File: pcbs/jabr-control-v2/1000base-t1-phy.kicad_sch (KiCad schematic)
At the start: 17 parts, among them U8001 LAN8870, Y8001 XRCGB25M000F3A16R0

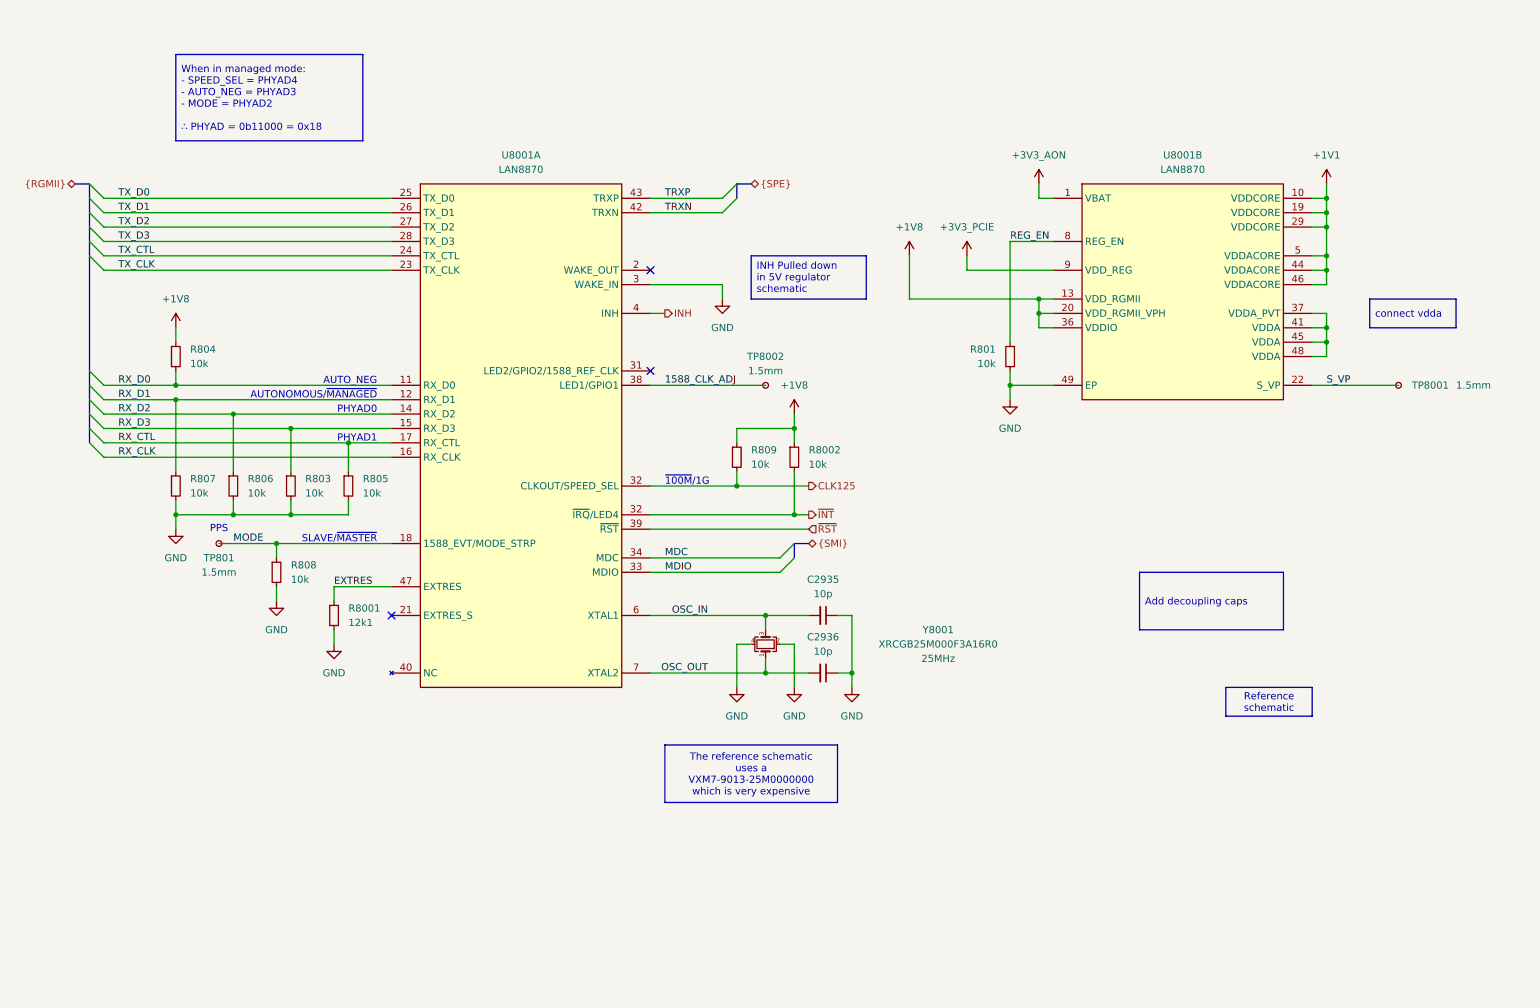
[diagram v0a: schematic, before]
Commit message: PCI11010C Schematic sheet mostly done
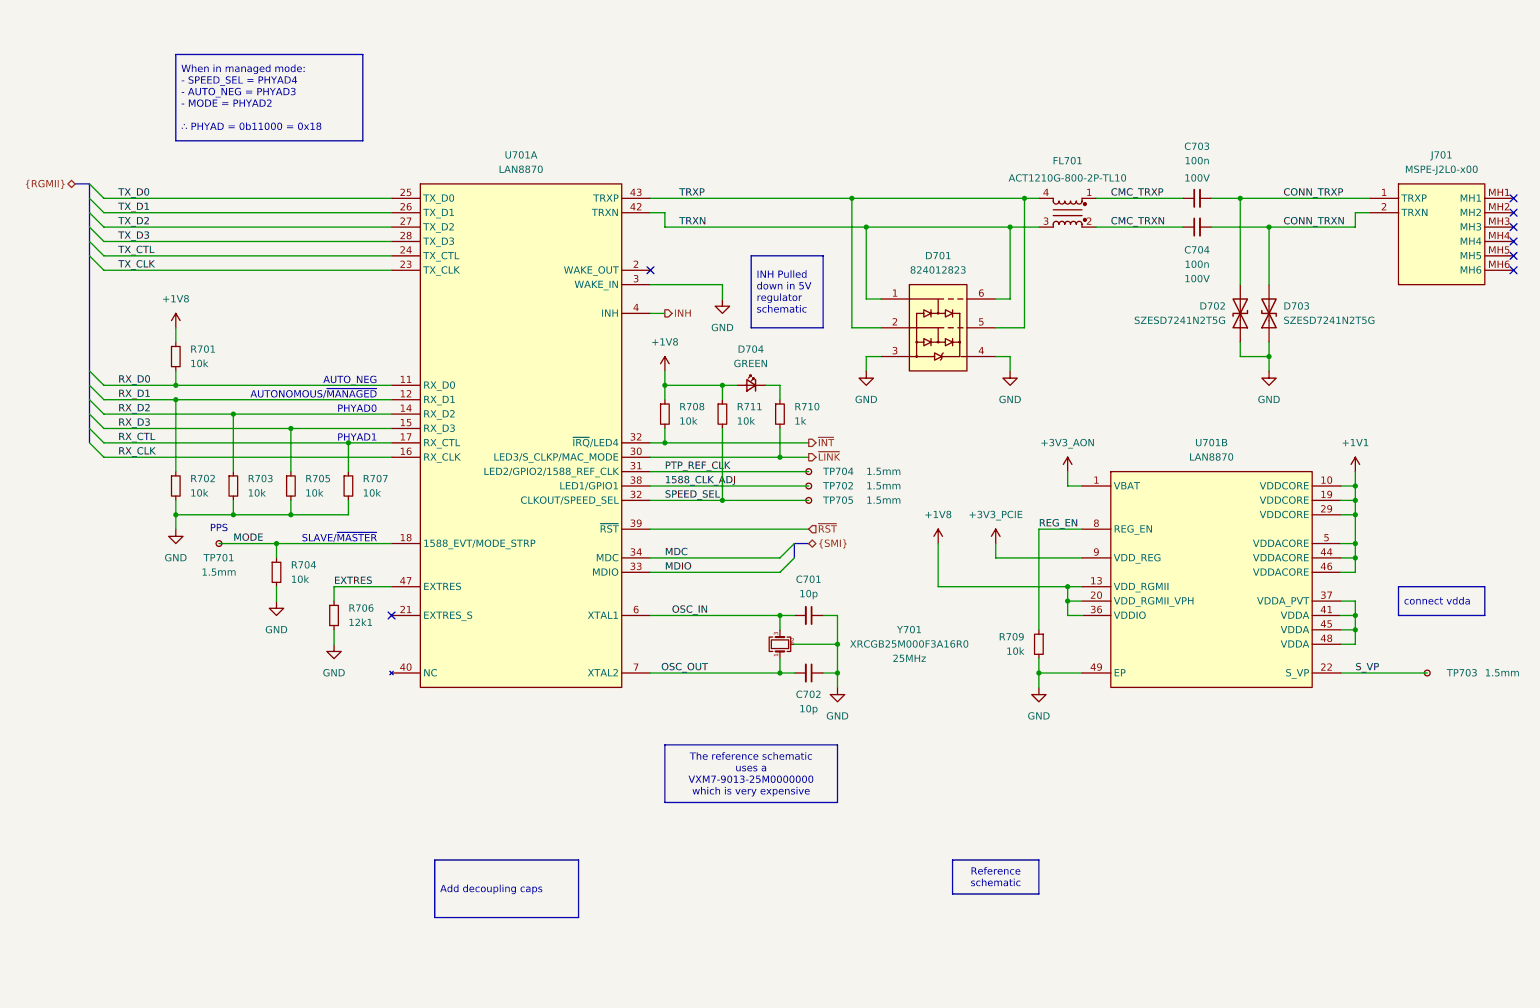
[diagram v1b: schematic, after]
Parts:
- removed R8002, R809: 10k, project_footprints:R_0402, symbol DEV:R_SMALL
- removed TP8002: 1.5mm, project_footprints:TestPoint_Pad_D1.5mm, symbol Connector:TestPoint_Small
- added C703, C704: 100n, project_footprints:C_0603, symbol DEV:C_SMALL
- added D701: 824012823, project_footprints:824012823, symbol TVS:824012823
- added D702, D703: SZESD7241N2T5G, project_footprints:SZESD7462N2T5G, symbol TVS:SZESD7241N2T5G
- added D704: GREEN, project_footprints:LED_0402, symbol DEV:LED_SMALL
- added FL701: ACT1210G-800-2P-TL10, project_footprints:ACT1210G, symbol COMM-CMC:ACT1210G-800-2P-TL10
- added J701: MSPE-J2L0-x00, project_footprints:MSPEJ2L0x00, symbol ETH-CONN:MSPE-J2L0-x00
- added R708, R711: 10k, project_footprints:R_0402, symbol DEV:R_SMALL
- added R710: 1k, project_footprints:R_0402, symbol DEV:R_SMALL
- added TP702, TP704, TP705: 1.5mm, project_footprints:TestPoint_Pad_D1.5mm, symbol Connector:TestPoint_Small
- renumbered C2935 to C701, C2936 to C702, R804 to R701, R807 to R702, R806 to R703, R808 to R704, R803 to R705, R8001 to R706, R805 to R707, R801 to R709, TP801 to TP701, TP8001 to TP703, U8001 to U701, Y8001 to Y701
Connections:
- net CLK125 is gone; now on net ~{INT}: U701.32 (CLKOUT/SPEED_SEL)
- net +1V8: now also D704.2 (A), R708.1, R711.1
- net 1588_CLK_ADJ: now also TP702.1
- net GND: now also D701.3, D701.4, D702.1 (A1), D703.1 (A1)
- net TRXN: now also D701.1, D701.6, FL701.3
- net TRXP: now also D701.2, D701.5, FL701.4
- net ~{INT}: now also R708.2
- net PTP_REF_CLK: now reaches U701.31 (LED2/GPIO2/1588_REF_CLK)
- net PTP_REF_CLK: now also TP704.1
- new net: D704.1 (K), R710.1
- new net CMC_TRXN: C704.1, FL701.2
- new net CMC_TRXP: C703.1, FL701.1
- new net CONN_TRXN: C704.2, D703.2 (A2), J701.2 (TRXN)
- new net CONN_TRXP: C703.2, D702.2 (A2), J701.1 (TRXP)
- new net SPEED_SEL: R711.2, TP705.1, U701.32 (CLKOUT/SPEED_SEL)
- new net ~{LINK}: R710.2, U701.30 (LED3/S_CLKP/MAC_MODE)
- no-connect marks 3 -> 8
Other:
- note removed: "~{100M}/1G"
- moved on the sheet: C701, C702, R709, TP703, U701B

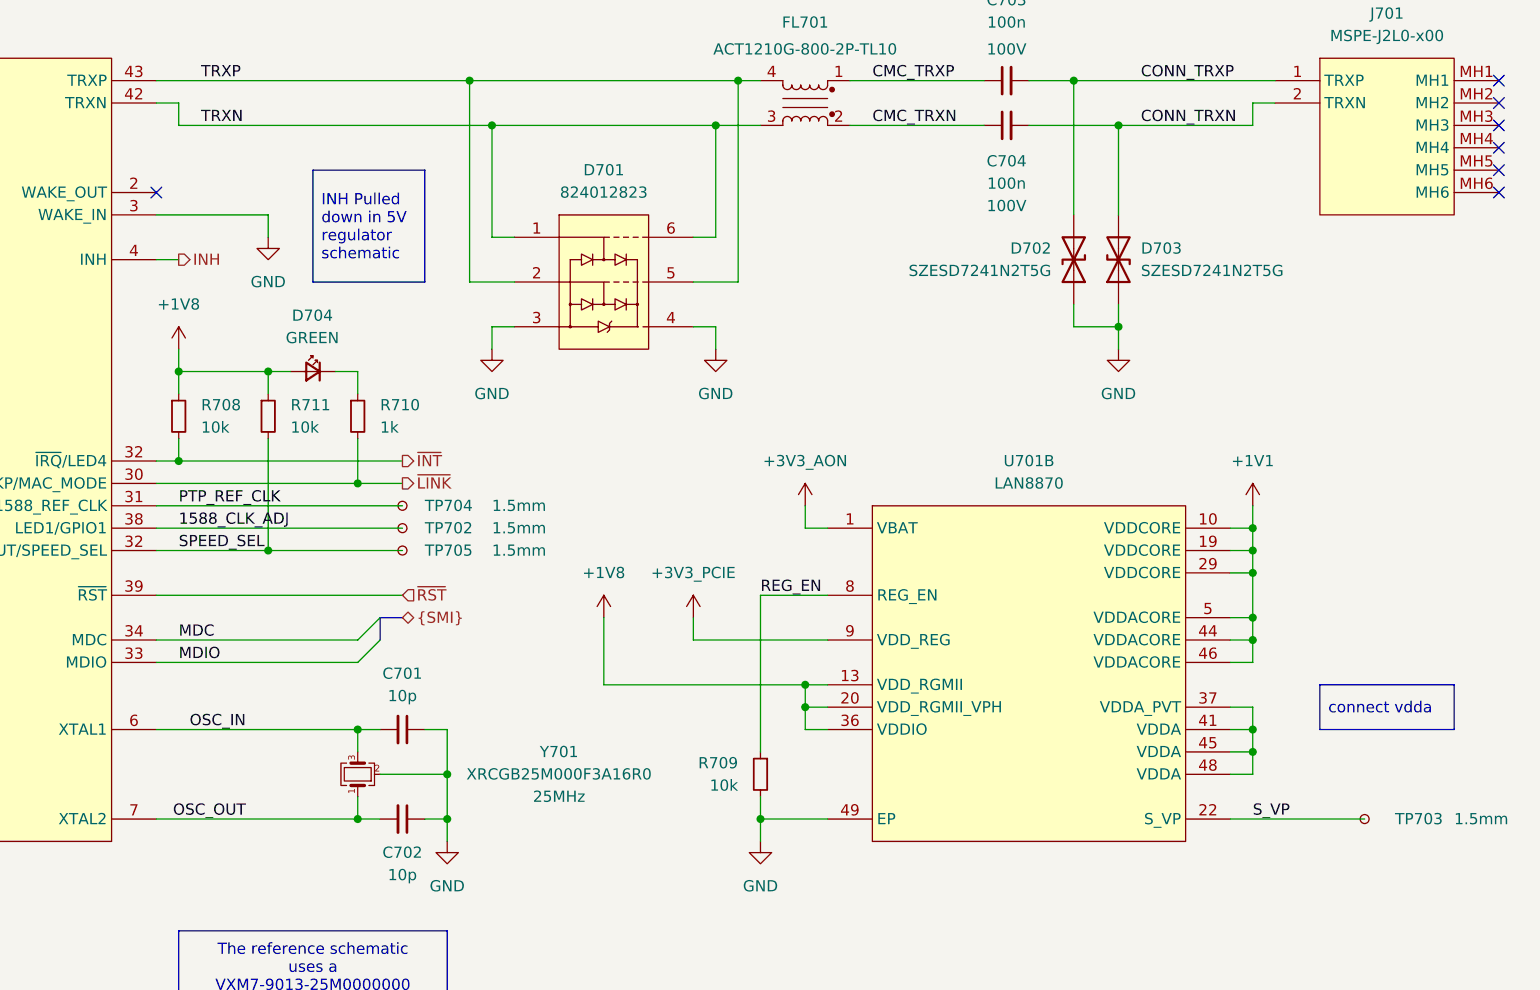
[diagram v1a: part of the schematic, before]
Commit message: Moved M.2 buffers to new sheet
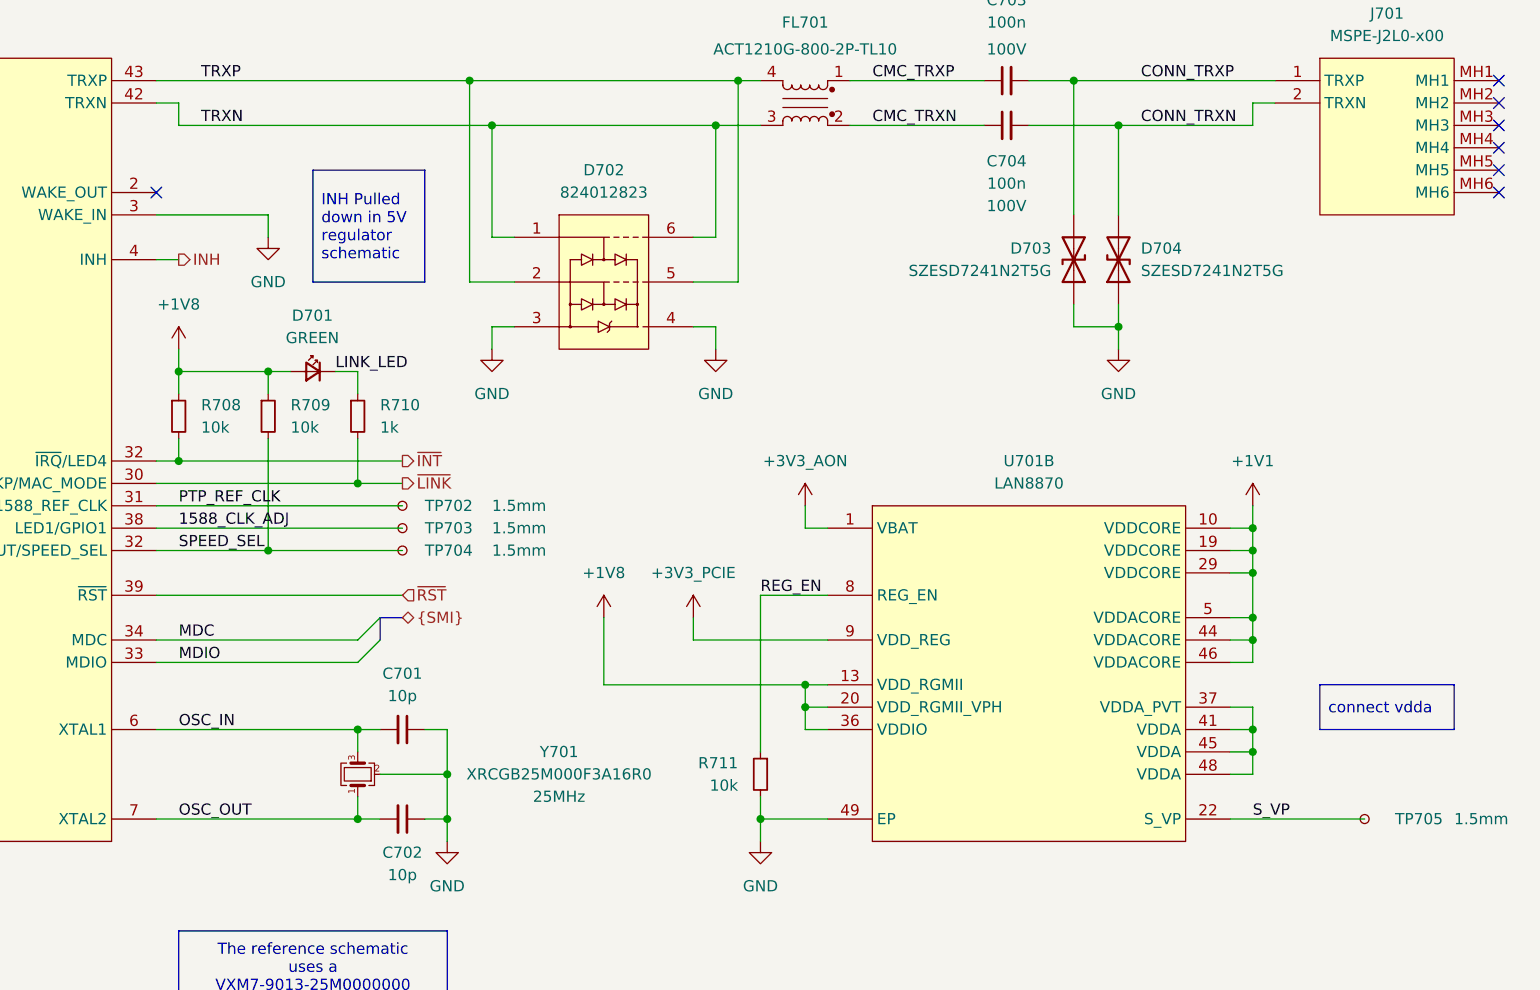
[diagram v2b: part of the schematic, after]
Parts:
- renumbered D704 to D701, D701 to D702, D702 to D703, D703 to D704, R711 to R709, R709 to R711, TP704 to TP702, TP702 to TP703, TP705 to TP704, TP703 to TP705
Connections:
- net LINK_LED: now reaches D701.1 (K), R710.1
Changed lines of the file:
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@@
 		)
 	)
+	(label "LINK_LED"
+		(at 147.32 86.36 0)
+		(effects
+			(font
+				(size 1.27 1.27)
+			)
+			(justify left bottom)
+		)
+	)
 	(label "MDIO"
 		(at 129.54 119.38 0)
@@
 	)
 	(label "OSC_OUT"
-		(at 137.16 137.16 180)
+		(at 129.54 137.16 0)
 		(effects
 			(font
 				(size 1.27 1.27)
 			)
-			(justify right bottom)
+			(justify left bottom)
 		)
 	)
 	(label "OSC_IN"
-		(at 137.16 127 180)
+		(at 129.54 127 0)
 		(effects
 			(font
 				(size 1.27 1.27)
 			)
-			(justify right bottom)
+			(justify left bottom)
 		)
 	)
@@
 		(length 2.54)
 		(shape round)
-		(at 137.16 127 180)
-		(fields_autoplaced yes)
-		(effects
-			(font
-				(size 1.27 1.27)
-			)
-			(justify right bottom)
-		)
-		(property "Net Class" "50Ω"
-			(at 136.4615 129.54 0)
-			(show_name no)
-			(do_not_autoplace no)
-			(effects
-				(font
-					(size 1.27 1.27)
-				)
-				(justify right)
-			)
-		)
-		(property "Component Class" ""
-			(at 317.5 40.64 0)
-			(show_name no)
-			(do_not_autoplace no)
-			(effects
-				(font
-					(size 1.27 1.27)
-					(italic yes)
-				)
-			)
-		)
-	)
-	(netclass_flag ""
-		(length 2.54)
-		(shape round)
-		(at 137.16 137.16 180)
-		(fields_autoplaced yes)
-		(effects
-			(font
-				(size 1.27 1.27)
-			)
-			(justify right bottom)
-		)
-		(property "Net Class" "50Ω"
-			(at 136.4615 139.7 0)
-			(show_name no)
-			(do_not_autoplace no)
-			(effects
-				(font
-					(size 1.27 1.27)
-				)
-				(justify right)
-			)
-		)
-		(property "Component Class" ""
-			(at 317.5 50.8 0)
-			(show_name no)
-			(do_not_autoplace no)
-			(effects
-				(font
-					(size 1.27 1.27)
-					(italic yes)
-				)
-			)
-		)
-	)
-	(netclass_flag ""
-		(length 2.54)
-		(shape round)
 		(at 27.94 50.8 0)
 		(fields_autoplaced yes)
@@
 		(dnp no)
 		(fields_autoplaced yes)
-		(property "Reference" "D704"
+		(property "Reference" "D701"
 			(at 144.7165 80.01 0)
 			(show_name no)
@@
 			(project "jabr-control-v2"
 				(path "/f91ec272-d09a-4038-bbbb-962739a92c51/760d12ad-9269-4cb7-9058-d98dd001df15"
-					(reference "D704")
+					(reference "D701")
 					(unit 1)
 				)
@@
 		(in_pos_files yes)
 		(dnp no)
-		(property "Reference" "D702"
+		(property "Reference" "D703"
 			(at 228.6 72.39 90)
 			(show_name no)
@@
 			(project "jabr-control-v2"
 				(path "/f91ec272-d09a-4038-bbbb-962739a92c51/760d12ad-9269-4cb7-9058-d98dd001df15"
-					(reference "D702")
+					(reference "D703")
 					(unit 1)
 				)
@@
 		(in_pos_files yes)
 		(dnp no)
-		(property "Reference" "R711"
+		(property "Reference" "R709"
 			(at 142.24 90.1699 0)
 			(show_name no)
@@
 			(project "jabr-control-v2"
 				(path "/f91ec272-d09a-4038-bbbb-962739a92c51/760d12ad-9269-4cb7-9058-d98dd001df15"
-					(reference "R711")
+					(reference "R709")
 					(unit 1)
 				)
@@
 		(in_pos_files yes)
 		(dnp no)
-		(property "Reference" "R709"
+		(property "Reference" "R711"
 			(at 193.04 130.8099 0)
 			(show_name no)
@@
 			(project "jabr-control-v2"
 				(path "/f91ec272-d09a-4038-bbbb-962739a92c51/760d12ad-9269-4cb7-9058-d98dd001df15"
-					(reference "R709")
+					(reference "R711")
 					(unit 1)
 				)
@@
 		(in_pos_files yes)
 		(dnp no)
-		(property "Reference" "TP704"
+		(property "Reference" "TP702"
 			(at 157.48 101.6 0)
 			(show_name no)
@@
 			(project "jabr-control-v2"
 				(path "/f91ec272-d09a-4038-bbbb-962739a92c51/760d12ad-9269-4cb7-9058-d98dd001df15"
-					(reference "TP704")
+					(reference "TP702")
 					(unit 1)
 				)
@@
 		(dnp no)
 		(fields_autoplaced yes)
-		(property "Reference" "#PWR0706"
+		(property "Reference" "#PWR0705"
 			(at 129.54 87.63 0)
 			(hide yes)
@@
 			(project "jabr-control-v2"
 				(path "/f91ec272-d09a-4038-bbbb-962739a92c51/760d12ad-9269-4cb7-9058-d98dd001df15"
-					(reference "#PWR0706")
+					(reference "#PWR0705")
 					(unit 1)
 				)
@@
 		(in_pos_files yes)
 		(dnp no)
-		(property "Reference" "TP703"
+		(property "Reference" "TP705"
 			(at 273.05 137.16 0)
 			(show_name no)
@@
 			(project "jabr-control-v2"
 				(path "/f91ec272-d09a-4038-bbbb-962739a92c51/760d12ad-9269-4cb7-9058-d98dd001df15"
-					(reference "TP703")
+					(reference "TP705")
 					(unit 1)
 				)
@@
 		(in_pos_files yes)
 		(dnp no)
-		(property "Reference" "TP705"
+		(property "Reference" "TP704"
 			(at 157.48 106.68 0)
 			(show_name no)
@@
 			(project "jabr-control-v2"
 				(path "/f91ec272-d09a-4038-bbbb-962739a92c51/760d12ad-9269-4cb7-9058-d98dd001df15"
-					(reference "TP705")
+					(reference "TP704")
 					(unit 1)
 				)
@@
 		(dnp no)
 		(fields_autoplaced yes)
-		(property "Reference" "D701"
+		(property "Reference" "D702"
 			(at 177.8 63.5 0)
 			(show_name no)
@@
 			(project "jabr-control-v2"
 				(path "/f91ec272-d09a-4038-bbbb-962739a92c51/760d12ad-9269-4cb7-9058-d98dd001df15"
-					(reference "D701")
+					(reference "D702")
 					(unit 1)
 				)
@@
 		(in_pos_files yes)
 		(dnp no)
-		(property "Reference" "TP702"
+		(property "Reference" "TP703"
 			(at 157.48 104.14 0)
 			(show_name no)
@@
 			(project "jabr-control-v2"
 				(path "/f91ec272-d09a-4038-bbbb-962739a92c51/760d12ad-9269-4cb7-9058-d98dd001df15"
-					(reference "TP702")
+					(reference "TP703")
 					(unit 1)
 				)
@@
 		(in_pos_files yes)
 		(dnp no)
-		(property "Reference" "D703"
+		(property "Reference" "D704"
 			(at 238.76 72.39 90)
 			(show_name no)
@@
 			(project "jabr-control-v2"
 				(path "/f91ec272-d09a-4038-bbbb-962739a92c51/760d12ad-9269-4cb7-9058-d98dd001df15"
-					(reference "D703")
+					(reference "D704")
 					(unit 1)
 				)
@@
 		(dnp no)
 		(fields_autoplaced yes)
-		(property "Reference" "#PWR0705"
+		(property "Reference" "#PWR0706"
 			(at 139.7 77.47 0)
 			(hide yes)
@@
 			(project "jabr-control-v2"
 				(path "/f91ec272-d09a-4038-bbbb-962739a92c51/760d12ad-9269-4cb7-9058-d98dd001df15"
-					(reference "#PWR0705")
+					(reference "#PWR0706")
 					(unit 1)
 				)
